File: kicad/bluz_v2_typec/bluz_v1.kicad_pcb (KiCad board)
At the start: 2 copper layers, 24.9 x 14.9 mm, 72 parts, among them J10 Conn, J11 Conn, J12 BTAnt, J2 Conn, J3 Conn, J4 Conn, J5 Conn, J6 Conn, J7 Conn, J8 Conn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

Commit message: изменено:      kicad/bluz_v2_typec/bluz_v1.kicad_pcb 	изменено:      kicad/bluz_v2_typec/bluz_v1.kicad_prl 	изменено:      kicad/bluz_v2_typec/bluz_v1.kicad_pro 	изменено:      kicad/bluz_v2_typec/bluz_v1.kicad_sch
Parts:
- removed BZ1: MLT-5020, lib:Buzzer55x55
- removed Q1: RUM002N05, My-library:SOT-723
- removed R11: 100k, Resistor_SMD:R_0402_1005Metric
- added BUZ1: PKMCS0909E4000-R1, easyeda2kicad:BUZ-SMD_L9.0-W9.0_PKMCS0909E4000-R1, F.Cu at (86.6, 42.5)
- added C27: 2.2u, Capacitor_SMD:C_0402_1005Metric, B.Cu at (87.0, 51.2)
- added C28: 1u, Capacitor_SMD:C_0402_1005Metric, F.Cu at (89.7, 51.3)
- added C29: 1u, Capacitor_SMD:C_0402_1005Metric, F.Cu at (86.9, 49.5)
- added U5: MCP1700-1.8, Package_TO_SOT_SMD:SOT-23-3, F.Cu at (79.5, 42.5)
- added U6: PAM8904EGPR, easyeda2kicad:W-QFN2020-12_L2.0-W2.0-P0.40-TL-EP0.9, F.Cu at (87.8, 51.4)
- C25: value 47n -> 2.2u
- C26, R1: moved to F.Cu
- R12, R5: moved to B.Cu
- moved C24 9.66 mm to (84.0, 52.6), turned to -90 degrees
- moved R1 9.09 mm to (85.0, 52.6)
- moved M1 5.40 mm to (81.0, 52.0), turned to -90 degrees
- moved C25 5.00 mm to (86.0, 52.6)
- moved R5 4.58 mm to (63.9, 53.0), turned to -90 degrees
- moved C26 4.51 mm to (83.0, 52.6), turned to 90 degrees
- moved Q2 2.42 mm to (83.2, 50.6), turned to -90 degrees
- moved R3 1.79 mm to (70.7, 50.2)
- moved J3 1.55 mm to (82.8, 43.4)
- moved C11 1.43 mm to (81.8, 39.0)
- moved J6 1.33 mm to (67.7, 52.1)
- moved J5 0.81 mm to (73.8, 48.3)
- moved J7 0.69 mm to (71.2, 52.0)
- moved R12 0.68 mm to (81.2, 43.4), turned to 0 degrees
- moved C23 0.55 mm to (76.8, 42.7)
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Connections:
- net Net-(D1-RST) renamed Rst
- C23 pad 1: +2V8 -> /1.8v
- C25 pad 2: Net-(BZ1-+) -> GND
- C8 pad 1: +2V8 -> /1.8v
- D1 pad 5: +2V8 -> /1.8v
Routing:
- net GND: track 154.6 -> 132.4 mm, vias 20 -> 23
- net Net-(U6-VO2): track 0.00 -> 13.0 mm
- net Sound: track 9.04 -> 19.7 mm, vias 1 -> 3
- net batLev: track 3.94 -> 12.5 mm, vias 0 -> 1
- net Net-(U6-VO1): track 0.00 -> 5.16 mm
- net Net-(BZ1-+): track 4.17 -> 0.00 mm
- net /1.8v: track 0.00 -> 3.44 mm, vias 0 -> 1
- net Net-(U6-CP1): track 0.00 -> 3.10 mm, vias 0 -> 2
- net Net-(LED1---Pad3): track 4.13 -> 1.15 mm, vias 1 -> 0
- net Net-(U6-CP2): track 0.00 -> 2.95 mm
- net /B+: track 2.50 -> 4.58 mm
- net +2V8: track 44.0 -> 41.9 mm, vias 7 -> 6
- net HVAdj: track 18.4 -> 17.0 mm
- net Net-(U1-PROG): track 1.06 -> 2.47 mm
- net Net-(U6-CN2): track 0.00 -> 1.15 mm
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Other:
- board size 24.9 x 14.9 mm -> 29.5 x 17.5 mm

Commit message: изменено:      Android/BluZ_LPM/BluZ/src/main/java/ru/starline/bluz/NumberFragment.kt 	изменено:      Android/BluZ_LPM/BluZ/src/main/java/ru/starline/bluz/drawSpecter.kt 	изменено:      Android/BluZ_LPM/BluZ/src/main/java/ru/starline/bluz/globalObj.kt 	изменено:      Android/BluZ_LPM/BluZ/src/main/res/layout/setup_layout.xml 	изменено:      kicad/bluz_v1_typec/bluz_v1.kicad_sch 	изменено:      kicad/bluz_v2_typec/bluz_v1.kicad_pcb 	изменено:      kicad/bluz_v2_typec/bluz_v1.kicad_pro 	изменено:      kicad/bluz_v2_typec/fp-info-cache 	изменено:      stm32cubeide/BluZ_LPM/BluZ_LPM.ioc 	изменено:      stm32cubeide/BluZ_LPM/Core/Src/main.c 	изменено:      stm32cubeide/BluZ_LPM/Release/BluZ_LPM.elf
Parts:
- moved J5 0.42 mm to (73.9, 47.9)
- moved J4 0.35 mm to (72.9, 47.0)
- moved R9 0.17 mm to (82.0, 48.8)
- moved J8 0.10 mm to (78.5, 46.0)
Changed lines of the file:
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@@
 	(footprint "lib:conn_mini"
 		(layer "B.Cu")
-		(at 72.72 47.28 180)
+		(at 72.922808 46.990205 180)
 		(property "Reference" "J4"
 			(at 0 0.5 0)
@@
 	(footprint "lib:conn_mini"
 		(layer "B.Cu")
-		(at 78.44 46.11 -90)
+		(at 78.497364 46.032502 -90)
 		(property "Reference" "J8"
 			(at 0.34 0.45 90)
@@
 	(footprint "lib:conn_mini"
 		(layer "B.Cu")
-		(at 73.75 48.27 180)
+		(at 73.911861 47.880935 180)
 		(property "Reference" "J5"
 			(at 0 0.5 0)
@@
 			)
 		)
+		(model "${KICAD9_3DMODEL_DIR}/Package_DFN_QFN.3dshapes/QFN-32-1EP_5x5mm_P0.5mm_EP3.3x3.3mm.wrl"
+			(offset
+				(xyz 0 0 0)
+			)
+			(scale
+				(xyz 1 1 1)
+			)
+			(rotate
+				(xyz 0 0 0)
+			)
+		)
 	)
 	(footprint "lib:conn_mini"
@@
 	(footprint "Resistor_SMD:R_0402_1005Metric"
 		(layer "B.Cu")
-		(at 81.97 48.61 90)
+		(at 81.97 48.782962 90)
 		(descr "Resistor SMD 0402 (1005 Metric), square (rectangular) end terminal, IPC_7351 nominal, (Body size source: IPC-SM-782 page 72, https://www.pcb-3d.com/wordpress/wp-content/uploads/ipc-sm-782a_amendment_1_and_2.pdf), generated with kicad-footprint-generator")
 		(tags "resistor")
@@
 	)
 	(segment
-		(start 81.95 49.27)
-		(end 80.97 49.27)
+		(start 81.95 49.340834)
+		(end 80.97 49.340834)
 		(width 0.25)
 		(layer "B.Cu")
@@
 	)
 	(segment
-		(start 79.04 47.18)
-		(end 79.04 46.16)
+		(start 79.074924 47.18)
+		(end 79.074924 46.16)
 		(width 0.25)
 		(layer "B.Cu")
@@
 	)
 	(segment
-		(start 78.334315 49.48)
-		(end 74.144214 49.48)
+		(start 72.09 43.425685)
+		(end 72.09 43.434315)
 		(width 0.2)
 		(layer "B.Cu")
@@
 	)
 	(segment
-		(start 72.207157 43.142843)
-		(end 72.412842 42.937158)
+		(start 71.43 44.425685)
+		(end 71.43 46.337199)
 		(width 0.2)
 		(layer "B.Cu")
@@
 	)
 	(segment
-		(start 71.547157 44.142843)
-		(end 71.972842 43.717158)
+		(start 71.722893 47.044306)
+		(end 73.865694 49.187107)
 		(width 0.2)
 		(layer "B.Cu")
@@
 	)
 	(segment
-		(start 71.43 46.765786)
-		(end 71.43 44.425685)
+		(start 71.972842 43.717158)
+		(end 71.547157 44.142843)
 		(width 0.2)
 		(layer "B.Cu")
@@
 	)
 	(segment
-		(start 72.695685 42.82)
-		(end 73.0725 42.82)
+		(start 74.572801 49.48)
+		(end 78.334315 49.48)
 		(width 0.2)
 		(layer "B.Cu")
@@
 	)
 	(segment
-		(start 78.64 49.34)
-		(end 78.617158 49.362842)
+		(start 78.617158 49.362842)
+		(end 78.64 49.34)
 		(width 0.2)
 		(layer "B.Cu")
@@
 	)
 	(segment
-		(start 73.437107 49.187107)
-		(end 71.722893 47.472893)
+		(start 72.412842 42.937158)
+		(end 72.207157 43.142843)
 		(width 0.2)
 		(layer "B.Cu")
@@
 	)
 	(segment
-		(start 72.09 43.434315)
-		(end 72.09 43.425685)
+		(start 73.0725 42.82)
+		(end 72.695685 42.82)
 		(width 0.2)
 		(layer "B.Cu")
@@
 	)
 	(arc
-		(start 72.09 43.425685)
+		(start 72.207157 43.142843)
 		(mid 72.120448 43.272612)
-		(end 72.207157 43.142843)
+		(end 72.09 43.425685)
 		(width 0.2)
 		(layer "B.Cu")
@@
 	)
 	(arc
-		(start 78.617158 49.362842)
+		(start 78.334315 49.48)
 		(mid 78.487389 49.449551)
-		(end 78.334315 49.48)
+		(end 78.617158 49.362842)
 		(width 0.2)
 		(layer "B.Cu")
@@
 	)
 	(arc
-		(start 72.412842 42.937158)
+		(start 72.695685 42.82)
 		(mid 72.542611 42.850449)
-		(end 72.695685 42.82)
+		(end 72.412842 42.937158)
 		(width 0.2)
 		(layer "B.Cu")
@@
 	)
 	(arc
-		(start 71.722893 47.472893)
-		(mid 71.50612 47.148469)
-		(end 71.43 46.765786)
+		(start 72.09 43.434315)
+		(mid 72.059552 43.587389)
+		(end 71.972842 43.717158)
 		(width 0.2)
 		(layer "B.Cu")
@@
 	)
 	(arc
-		(start 71.43 44.425685)
+		(start 71.547157 44.142843)
 		(mid 71.460448 44.272612)
-		(end 71.547157 44.142843)
+		(end 71.43 44.425685)
 		(width 0.2)
 		(layer "B.Cu")
@@
 	)
 	(arc
-		(start 73.437107 49.187107)
-		(mid 73.76153 49.40388)
-		(end 74.144214 49.48)
+		(start 71.43 46.337199)
+		(mid 71.50612 46.719882)
+		(end 71.722893 47.044306)
 		(width 0.2)
 		(layer "B.Cu")
@@
 	)
 	(arc
-		(start 71.972842 43.717158)
-		(mid 72.059552 43.587389)
-		(end 72.09 43.434315)
+		(start 74.572801 49.48)
+		(mid 74.190118 49.40388)
+		(end 73.865694 49.187107)
 		(width 0.2)
 		(layer "B.Cu")
@@
 	)
 	(via
-		(at 71.58 48.53)
+		(at 71.67 48.44)
 		(size 0.6)
 		(drill 0.3)
@@
 	)
 	(segment
-		(start 72.29 44.795685)
-		(end 72.29 45.245786)
+		(start 72.482842 44.437158)
+		(end 72.407157 44.512843)
 		(width 0.2)
 		(layer "B.Cu")
@@
 	)
 	(segment
-		(start 73.75 47.534214)
-		(end 73.75 48.27)
+		(start 73.576019 46.324677)
+		(end 73.736125 46.484783)
 		(width 0.2)
 		(layer "B.Cu")
@@
 	)
 	(segment
-		(start 73.0725 44.32)
-		(end 72.765685 44.32)
+		(start 72.465736 45.76008)
+		(end 72.678861 45.973205)
 		(width 0.2)
 		(layer "B.Cu")
@@
 	)
 	(segment
-		(start 72.582893 45.952893)
-		(end 73.457107 46.827107)
+		(start 73.911861 46.909047)
+		(end 73.911861 47.880935)
 		(width 0.2)
 		(layer "B.Cu")
@@
 	)
 	(segment
-		(start 72.482842 44.437158)
-		(end 72.407157 44.512843)
+		(start 73.103125 46.148941)
+		(end 73.151755 46.148941)
+		(width 0.2)
+		(layer "B.Cu")
+		(net 42)
+	)
+	(segment
+		(start 72.29 44.795685)
+		(end 72.29 45.335816)
+		(width 0.2)
+		(layer "B.Cu")
+		(net 42)
+	)
+	(segment
+		(start 73.0725 44.32)
+		(end 72.765685 44.32)
 		(width 0.2)
 		(layer "B.Cu")
@@
 	)
 	(arc
-		(start 73.457107 46.827107)
-		(mid 73.67388 47.15153)
-		(end 73.75 47.534214)
+		(start 73.151755 46.148941)
+		(mid 73.381365 46.194613)
+		(end 73.576019 46.324677)
 		(width 0.2)
 		(layer "B.Cu")
@@
 	)
 	(arc
-		(start 72.407157 44.512843)
-		(mid 72.320448 44.642612)
-		(end 72.29 44.795685)
+		(start 72.465736 45.76008)
+		(mid 72.335672 45.565426)
+		(end 72.29 45.335816)
+		(width 0.2)
+		(layer "B.Cu")
+		(net 42)
+	)
+	(arc
+		(start 73.911861 46.909047)
+		(mid 73.866189 46.679437)
+		(end 73.736125 46.484783)
+		(width 0.2)
+		(layer "B.Cu")
+		(net 42)
+	)
+	(arc
+		(start 73.103125 46.148941)
+		(mid 72.873515 46.103269)
+		(end 72.678861 45.973205)
 		(width 0.2)
 		(layer "B.Cu")
@@
 	)
 	(arc
-		(start 72.582893 45.952893)
-		(mid 72.36612 45.62847)
-		(end 72.29 45.245786)
+		(start 72.407157 44.512843)
+		(mid 72.320448 44.642612)
+		(end 72.29 44.795685)
 		(width 0.2)
 		(layer "B.Cu")

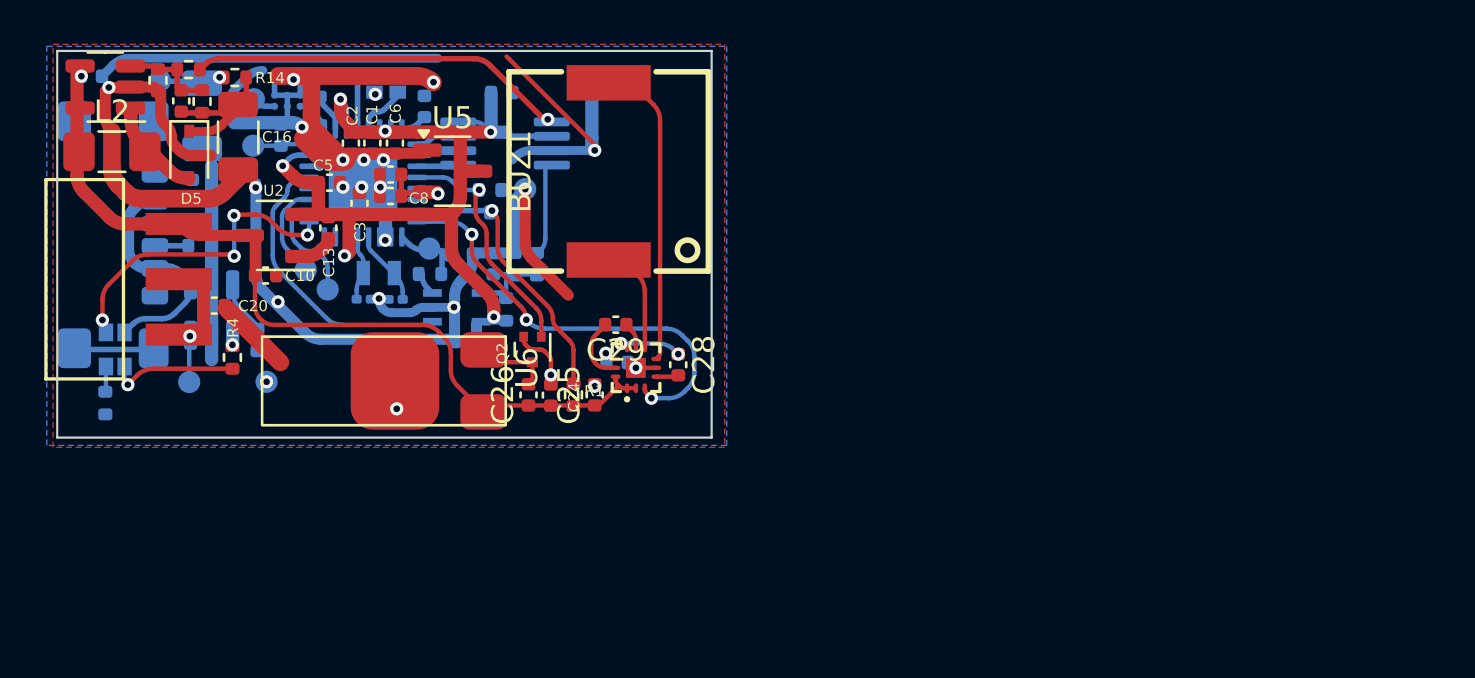
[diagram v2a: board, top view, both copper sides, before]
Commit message: удалено:       kicad/bluz_v2_typec/bluz_v1-backups/bluz_v1-2025-11-02_134433.zip 	удалено:       kicad/bluz_v2_typec/bluz_v1-backups/bluz_v1-2025-11-02_135440.zip 	изменено:      kicad/bluz_v2_typec/bluz_v1.kicad_pcb 	изменено:      kicad/bluz_v2_typec/bluz_v1.kicad_prl 	удалено:       kicad/bluz_v2_typec/gerber/BluZ.zip
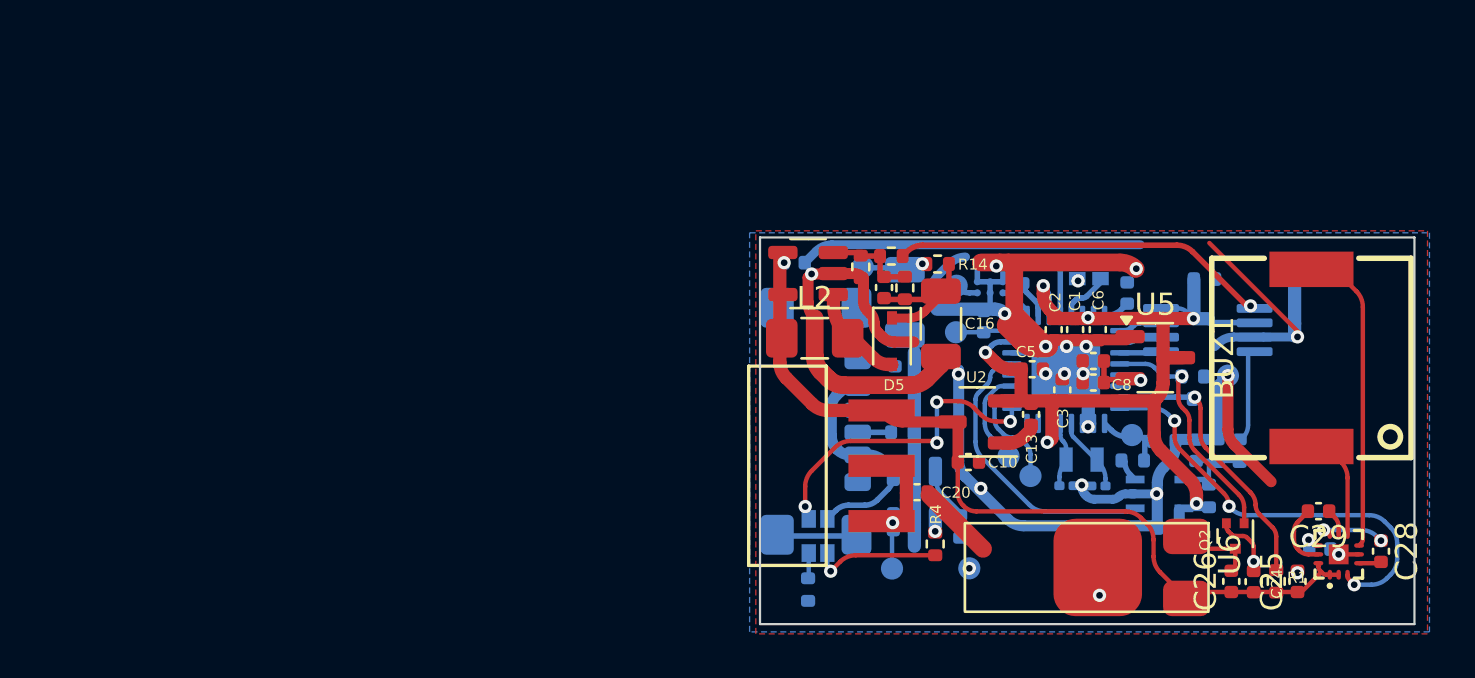
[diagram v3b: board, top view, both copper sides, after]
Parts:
- moved BUZ1 32.8 mm to (118.3, 51.0)
- moved C11 32.8 mm to (113.5, 47.4)
- moved C13 32.8 mm to (105.7, 53.5)
- moved C14 32.8 mm to (111.9, 58.7)
- moved C18 32.8 mm to (103.5, 49.3)
- moved C19 32.8 mm to (100.0, 48.5)
- moved C2 32.8 mm to (106.7, 49.7)
- moved C24 32.8 mm to (115.7, 61.1)
- moved C25 32.8 mm to (117.7, 61.1)
- moved C28 32.8 mm to (121.5, 59.7)
- moved C3 32.8 mm to (107.1, 52.4)
- moved C5 32.8 mm to (105.7, 51.5)
- moved C9 32.8 mm to (99.0, 47.8)
- moved D5 32.8 mm to (99.4, 50.2)
- moved J10 32.8 mm to (101.3, 51.3)
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
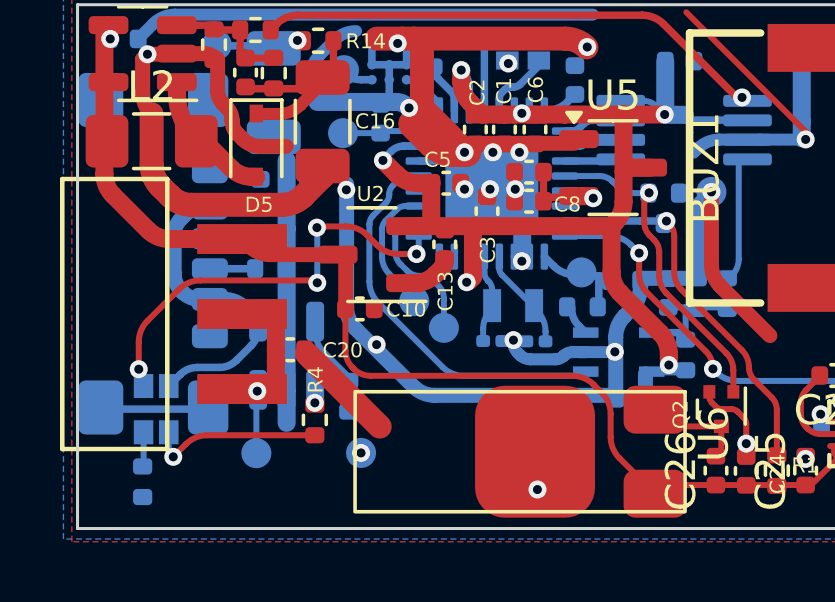
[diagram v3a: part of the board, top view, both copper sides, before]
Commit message: удалено:       kicad/bluz_v2_typec/bluz_v1-backups/bluz_v1-2025-11-02_152254.zip 	удалено:       kicad/bluz_v2_typec/bluz_v1-backups/bluz_v1-2025-11-22_184209.zip 	удалено:       kicad/bluz_v2_typec/bluz_v1-backups/bluz_v1-2025-11-25_161346.zip 	удалено:       kicad/bluz_v2_typec/bluz_v1-backups/bluz_v1-2025-11-25_161928.zip 	удалено:       kicad/bluz_v2_typec/bluz_v1-backups/bluz_v1-2025-11-25_163739.zip 	изменено:      kicad/bluz_v2_typec/bluz_v1.kicad_pcb 	изменено:      kicad/bluz_v2_typec/bluz_v1.kicad_prl
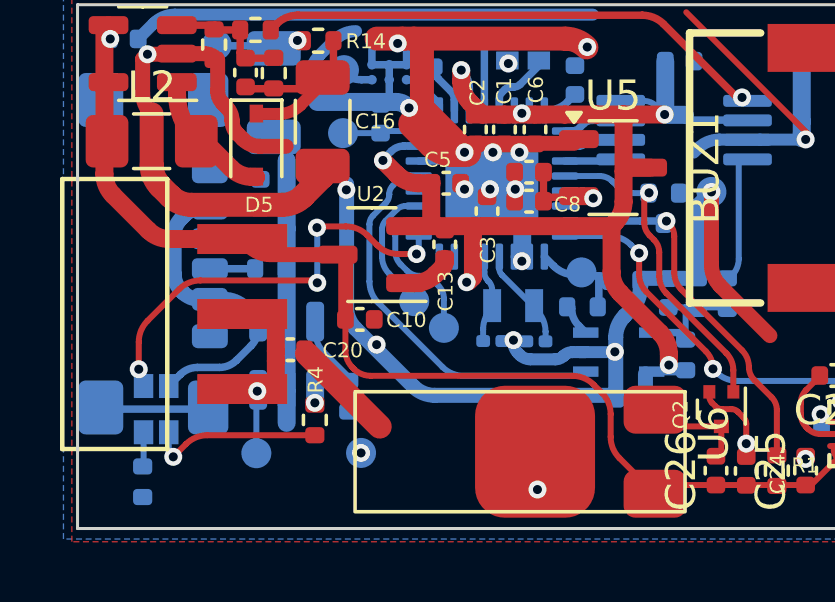
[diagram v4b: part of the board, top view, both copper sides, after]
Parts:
- moved C10 0.35 mm to (102.8, 56.0)
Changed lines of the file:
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@@
 	(footprint "Capacitor_SMD:C_0402_1005Metric"
 		(layer "F.Cu")
-		(at 102.843128 55.67226)
+		(at 102.843128 56.022055)
 		(descr "Capacitor SMD 0402 (1005 Metric), square (rectangular) end terminal, IPC_7351 nominal, (Body size source: IPC-SM-782 page 76, https://www.pcb-3d.com/wordpress/wp-content/uploads/ipc-sm-782a_amendment_1_and_2.pdf), generated with kicad-footprint-generator")
 		(tags "capacitor")

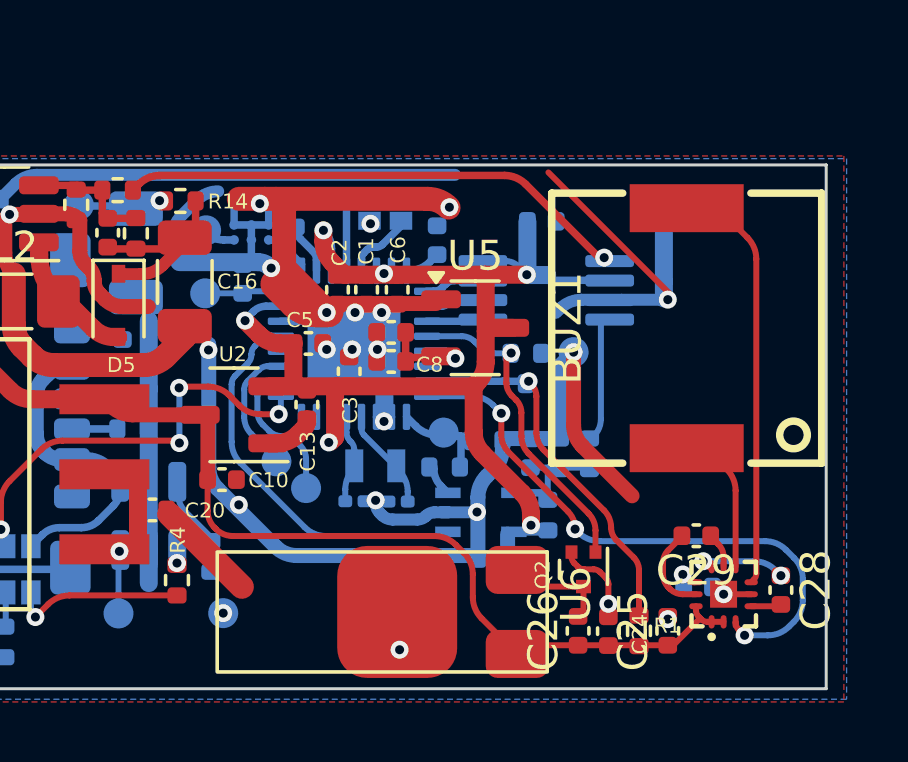
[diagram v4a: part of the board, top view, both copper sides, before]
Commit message: изменено:      Android/BluZ_LPM/BluZ/src/main/java/ru/starline/bluz/BluetoothInterface.kt 	удалено:       kicad/bluz_v2_typec/bluz_v1-backups/bluz_v1-2025-11-25_164259.zip 	удалено:       kicad/bluz_v2_typec/bluz_v1-backups/bluz_v1-2025-11-25_165421.zip 	удалено:       kicad/bluz_v2_typec/bluz_v1-backups/bluz_v1-2025-11-29_144245.zip 	удалено:       kicad/bluz_v2_typec/bluz_v1-backups/bluz_v1-2026-01-22_200222.zip 	изменено:      kicad/bluz_v2_typec/bluz_v1.kicad_pcb 	изменено:      kicad/bluz_v2_typec/bluz_v1.kicad_prl 	изменено:      kicad/bluz_v2_typec/bluz_v1.kicad_sch 	изменено:      stm32cubeide/BluZ_LPM/BluZ_LPM_v1.ioc 	изменено:      stm32cubeide/BluZ_LPM/Core/Src/main.c 	изменено:      stm32cubeide/BluZ_LPM/Release/BluZ_LPM_v1.elf 	изменено:      stm32cubeide/BluZ_archive/.settings/language.settings.xml
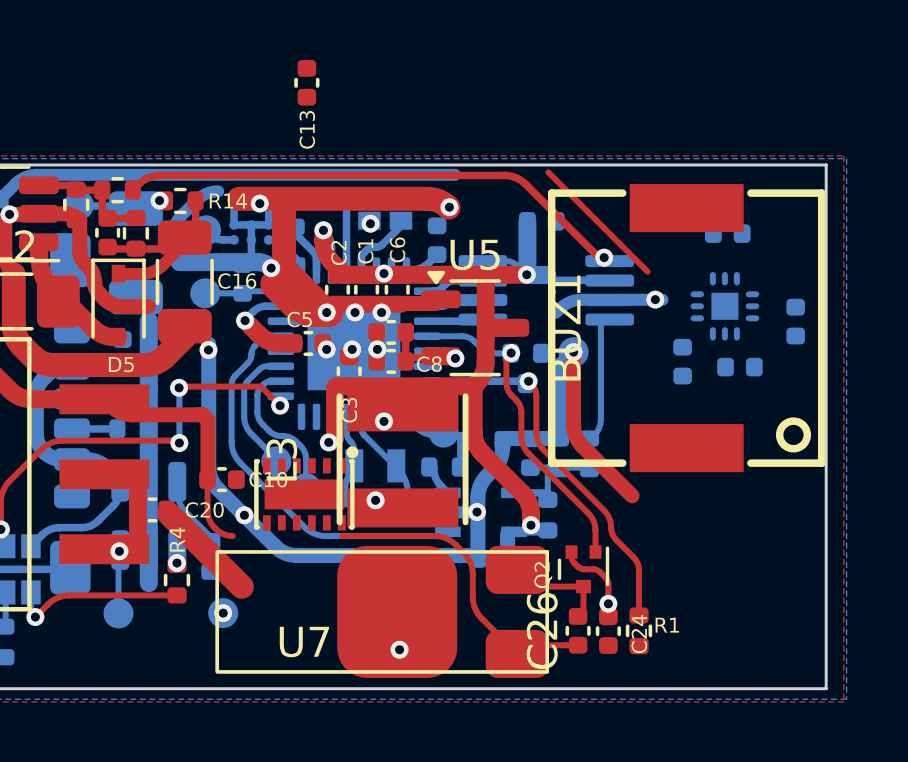
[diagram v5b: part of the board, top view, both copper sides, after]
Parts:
- removed U2: MCP1700, Package_TO_SOT_SMD:SOT-23-3
- added L3: SRN4018-6R8M, easyeda2kicad:IND-SMD_L4.0-W4.0_SMNR4018, F.Cu at (108.9, 55.4)
- added U7: TPS627451DSSR, easyeda2kicad:WSON-12_L3.0-W2.0-P0.5-BL-EP, F.Cu at (105.6, 56.5)
- C25, C28, C29, U6: moved to B.Cu
- moved C28 12.0 mm to (119.7, 47.8), turned to 180 degrees
- moved C13 10.7 mm to (105.7, 42.8)
- moved U6 9.60 mm to (119.6, 50.2), turned to 0 degrees
- moved C27 9.43 mm to (122.0, 50.8), turned to 90 degrees
- moved C25 8.99 mm to (118.2, 52.1), turned to -90 degrees
- moved C29 5.80 mm to (120.1, 52.3)
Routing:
- net Sound: track 19.7 -> 0.00 mm, vias 3 -> 0
- net Net-(U6-VO2): track 13.0 -> 0.00 mm
- net +BATT: track 39.4 -> 30.0 mm
- net GND: track 132.4 -> 126.0 mm, vias 23 -> 21
- net Net-(U6-VO1): track 5.16 -> 0.00 mm
- net +2V8: track 41.9 -> 38.7 mm
- net Net-(U6-CP1): track 3.10 -> 0.00 mm, vias 2 -> 0
- net Net-(U6-CP2): track 2.95 -> 0.00 mm
- net Net-(U6-CN2): track 1.15 -> 0.00 mm
- net Net-(U6-CN1): track 1.01 -> 0.00 mm
- net Net-(U6-VOUT): track 0.53 -> 0.00 mm, vias 1 -> 0
